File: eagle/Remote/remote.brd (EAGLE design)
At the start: 55 x 55 mm, 29 parts, among them U1 ATTINY84-20SSU

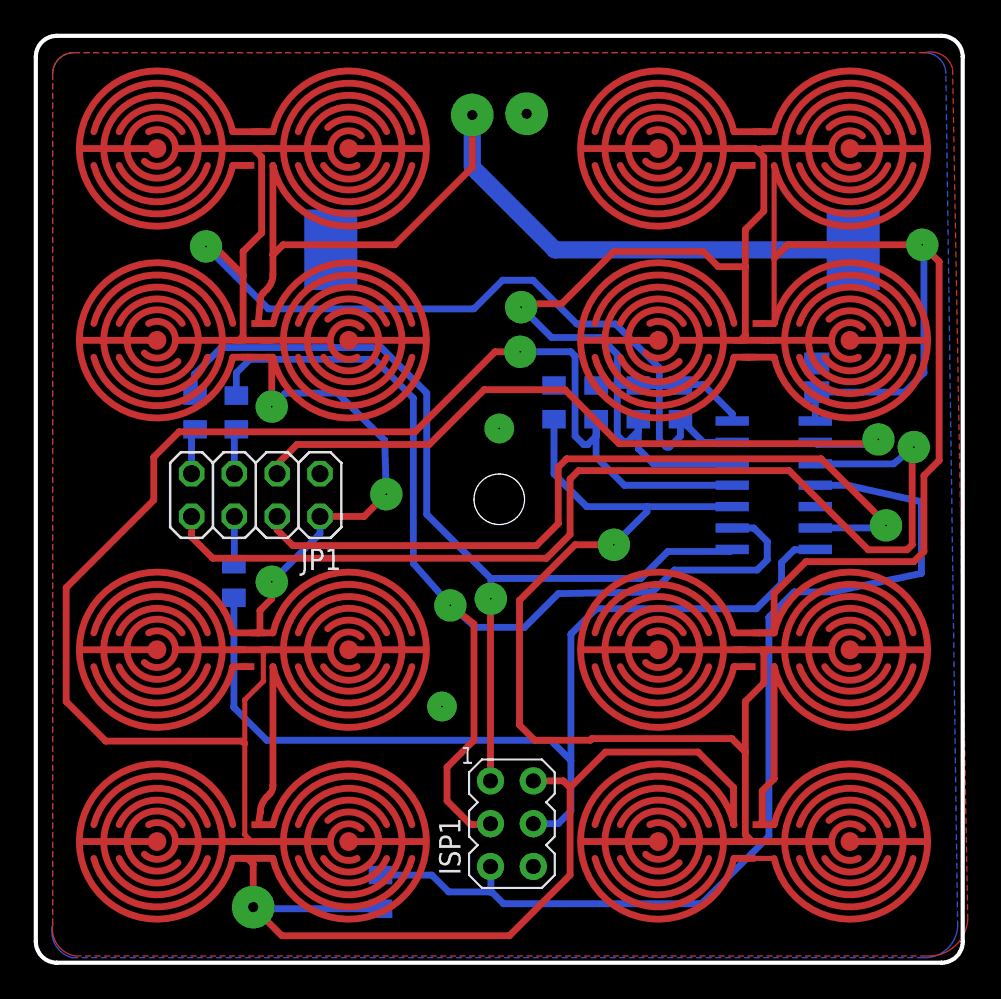
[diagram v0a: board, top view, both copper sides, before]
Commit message: remote brd fixes (ISP, pulldowns, GND)
This mirrors the ISP header so it is accessible in the proper
configuration under the board.  It also fixes the some bridging between
ground and signal from the buttons
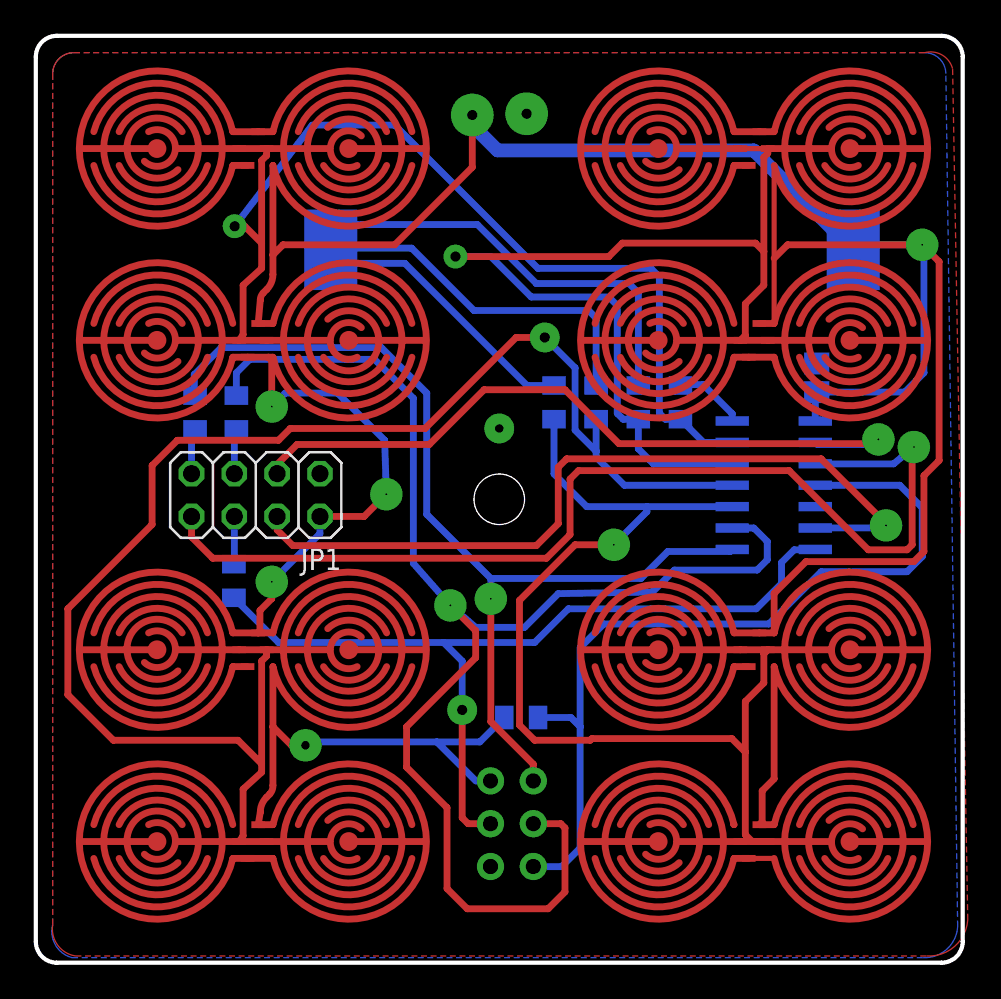
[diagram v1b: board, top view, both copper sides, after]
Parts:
- moved R8 13.3 mm to (28.8, 14.6), turned to 180 degrees
- flipped ISP1 to the bottom
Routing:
- net GND: track 9.24 -> 68.4 mm, vias 3 -> 2
- net VCC: track 231.9 -> 200.9 mm
- net SCK: track 66.8 -> 85.0 mm
- net RESET: track 60.4 -> 50.2 mm
- net BUTTON2: track 53.1 -> 60.4 mm
- net MOSI: track 58.2 -> 51.3 mm, vias 0 -> 1
- net BUTTON1: track 61.1 -> 62.4 mm
- net MISO: track 56.5 -> 57.5 mm
- net BUTTON3: track 90.6 -> 89.7 mm
